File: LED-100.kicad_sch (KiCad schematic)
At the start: 100 parts, among them J2 LDA100_2_J2, J3 LDA100_2_J3, J4 LDA100_2_J4, J5 xtra, J7 Conn_01x01, J8 Conn_01x06, SW1 SW_SPDT, U1 TLC5947DAP, U2 TLC5947DAP, U3 TLC5947DAP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

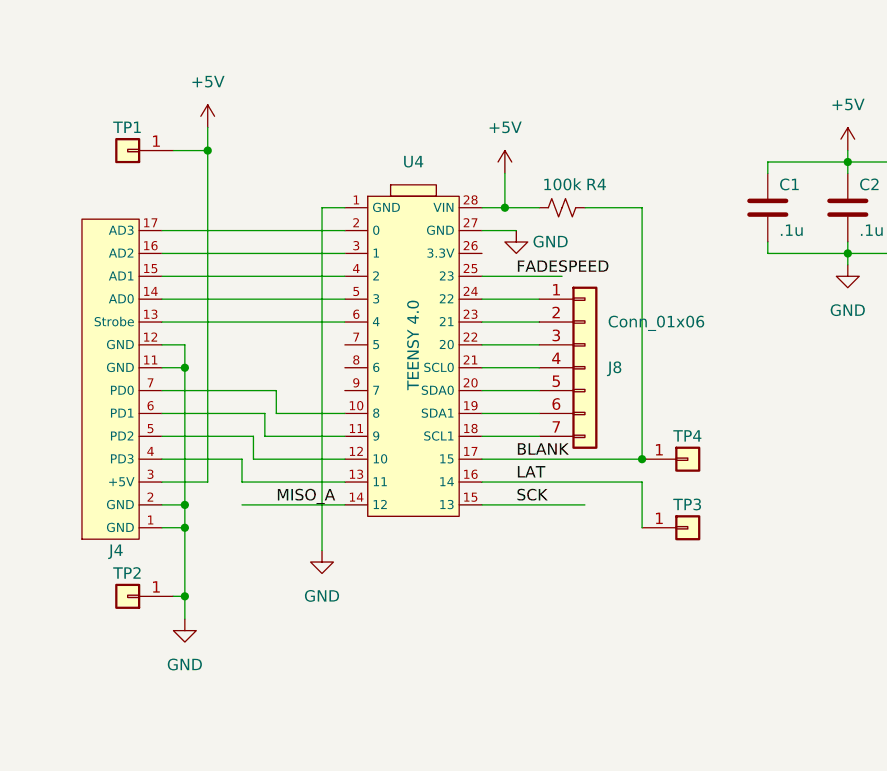
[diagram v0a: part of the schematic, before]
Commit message: diagonal teensy, pin reassignments, tweaks
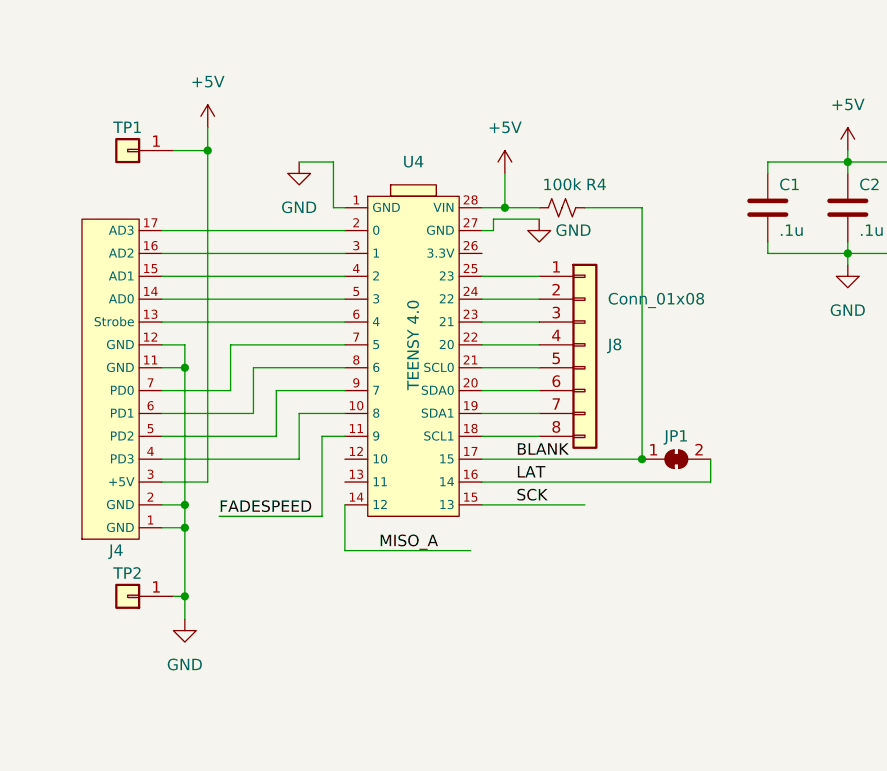
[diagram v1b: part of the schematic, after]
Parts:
- removed TP3, TP4: Conn_01x01, Connector_PinHeader_2.54mm:PinHeader_1x01_P2.54mm_Vertical, symbol Connector_Generic:Conn_01x01
- added JP1: SolderJumper_2_Bridged, Jumper:SolderJumper-2_P1.3mm_Bridged_Pad1.0x1.5mm, symbol Jumper:SolderJumper_2_Bridged
- J8: value Conn_01x06 -> Conn_01x08; footprint Connector_PinHeader_2.54mm:PinHeader_1x07_P2.54mm_Vertical -> Connector_PinHeader_2.54mm:PinHeader_1x08_P2.54mm_Vertical; symbol Connector_Generic:Conn_01x07 -> Connector_Generic:Conn_01x08
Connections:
- net BLANK: now also JP1.1 (A)
- net FADESPEED: now also U4.11 (9); no longer U4.25 (23)
- net LAT: now also JP1.2 (B)
- net at U4.10 (8): now also J4.4 (PD3); no longer J4.7 (PD0)
- net at J4.6 (PD1): now also U4.8 (6); no longer U4.11 (9)
- net at U4.12 (10): no longer J4.5 (PD2)
- net at U4.13 (11): no longer J4.4 (PD3)
- net at U4.18 (SCL1): now also J8.8 (Pin_8); no longer J8.7 (Pin_7)
- net at U4.19 (SDA1): now also J8.7 (Pin_7); no longer J8.6 (Pin_6)
- net at U4.20 (SDA0): now also J8.6 (Pin_6); no longer J8.5 (Pin_5)
- net at U4.21 (SCL0): now also J8.5 (Pin_5); no longer J8.4 (Pin_4)
- net at U4.22 (20): now also J8.4 (Pin_4); no longer J8.3 (Pin_3)
- net at U4.23 (21): now also J8.3 (Pin_3); no longer J8.2 (Pin_2)
- net at U4.24 (22): now also J8.2 (Pin_2); no longer J8.1 (Pin_1)
- net at U4.7 (5): now also J4.7 (PD0)
- net at U4.9 (7): now also J4.5 (PD2)
- new net: J8.1 (Pin_1), U4.25 (23)

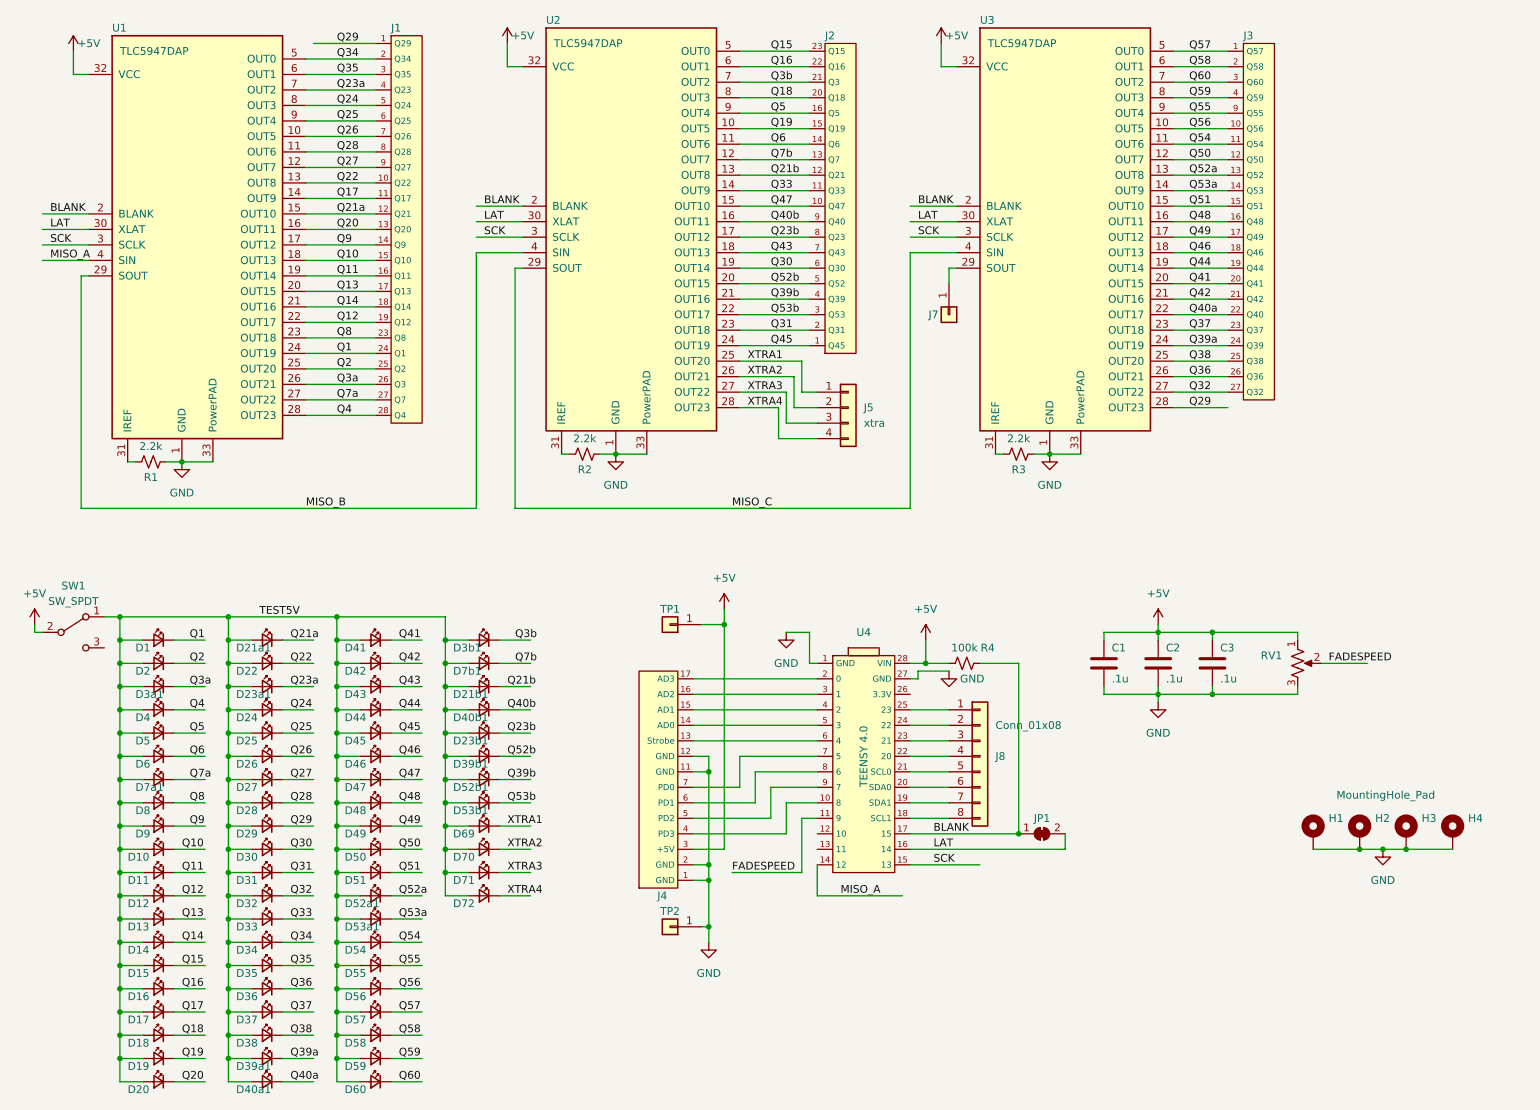
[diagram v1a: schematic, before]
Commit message: added a switch, updated to kicad 9
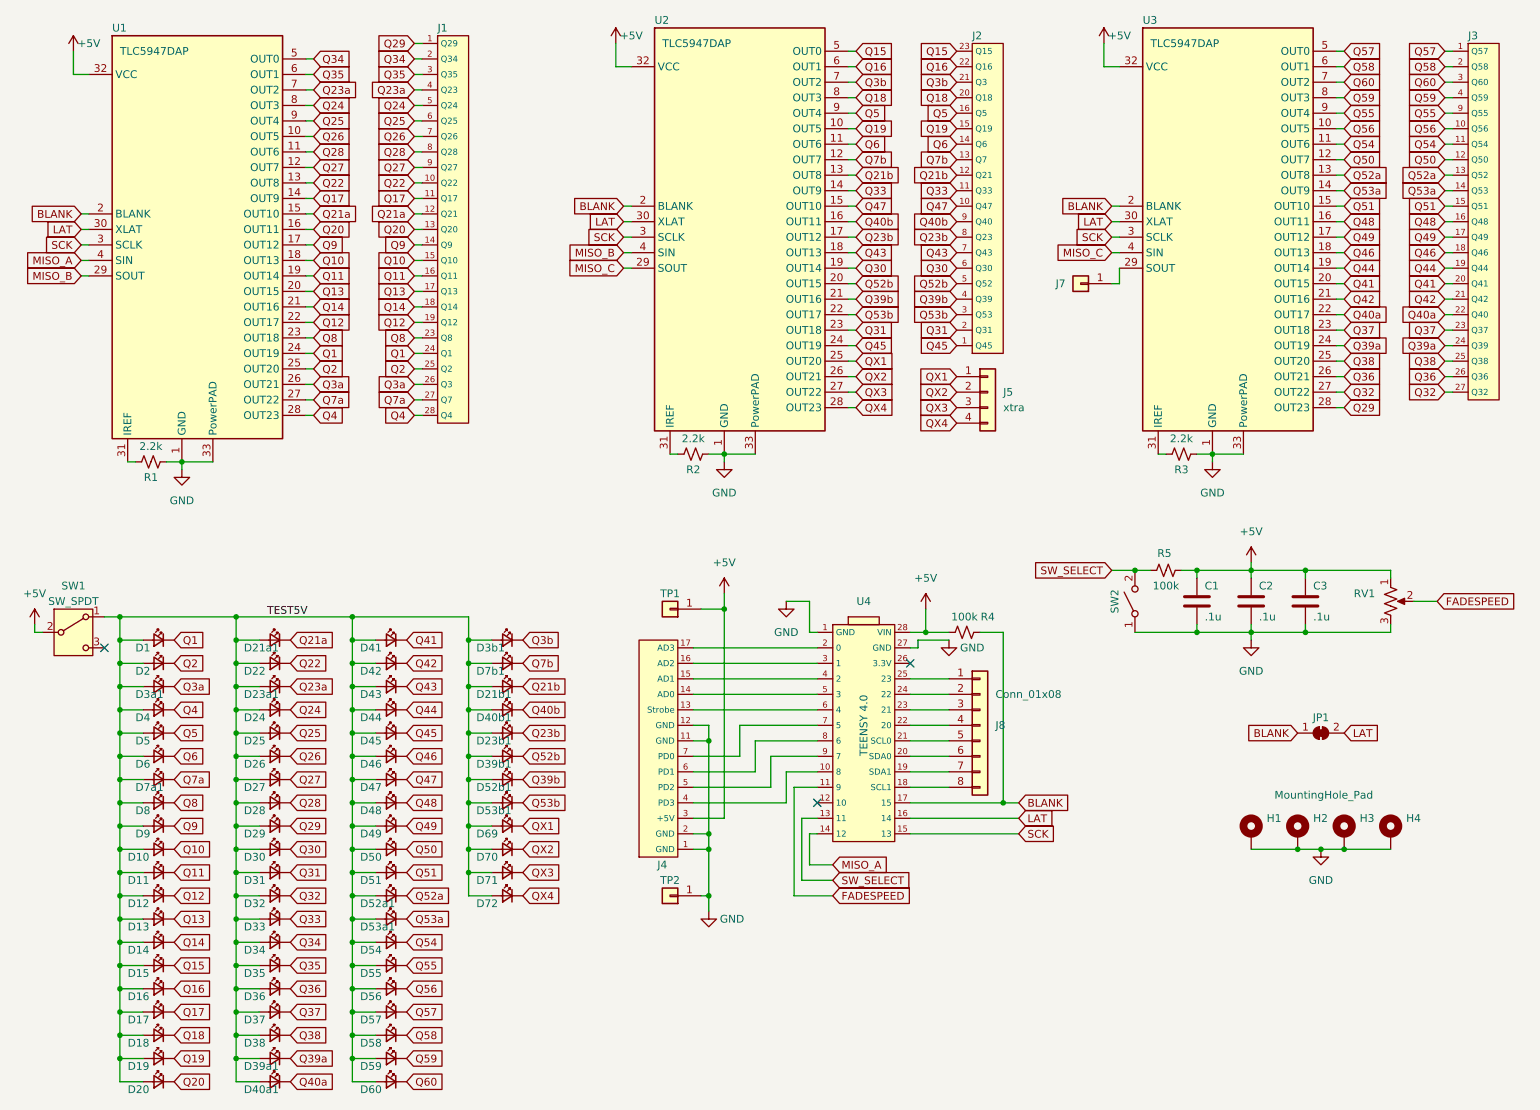
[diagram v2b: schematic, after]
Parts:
- added R5: 100k, Resistor_THT:R_Axial_DIN0204_L3.6mm_D1.6mm_P5.08mm_Horizontal, symbol Device:R_Small_US
- added SW2: SW_SPST, Button_Switch_THT:SW_PUSH_6mm_H5mm, symbol Switch:SW_SPST
- J1: symbol F2K_Library:LDA100_2_J1 -> LED-100_Library:LDA100_2_J1
- J2: symbol F2K_Library:LDA100_2_J2 -> LED-100_Library:LDA100_2_J2
- J3: symbol F2K_Library:LDA100_2_J3 -> LED-100_Library:LDA100_2_J3
- J4: symbol F2K_Library:LDA100_2_J4 -> LED-100_Library:LDA100_2_J4
- SW1: footprint Button_Switch_THT:SW_Slide_SPDT_SLW-12689-4A-N-D -> MyParts:SWITCH_SPDT-SLW-12689-4A-N-D
- U1, U2, U3: footprint Package_SO:HTSSOP-32-1EP_6.1x11mm_P0.65mm_EP5.2x11mm_Mask4.11x4.36mm_ThermalVias -> MyParts:Package_SO_HTSSOP-32-1EP_6.1x11mm_P0.65mm_EP5.2x11mm_Mask4.11x4.36mm_ThermalVias; symbol Driver_LED:TLC5947DAP -> MySymbols:TLC5947
- U4: footprint Connector_PinHeader_2.54mm:PinHeader_2x1x14_P2.54mm_Vertical -> MyParts:Teensy 4.0; symbol F2K_Library:Teensy_4.0_headers -> LED-100_Library:Teensy_4.0_headers
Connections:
- net +5V: now also R5.1
- net GND: now also SW2.1 (A)
- net SW_SELECT: now reaches U4.13 (11)
- net SW_SELECT: now also R5.2, SW2.2 (B)
- net XTRA1 renamed QX1
- net XTRA2 renamed QX2
- net XTRA3 renamed QX3
- net XTRA4 renamed QX4
- no-connect marks 0 -> 3
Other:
- moved on the sheet: C1, C2, C3, D21a1, D21b1, D22, D23a1, D23b1, D24, D25, D26, D27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
